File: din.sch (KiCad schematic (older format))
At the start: 1 part, among them J100 C96

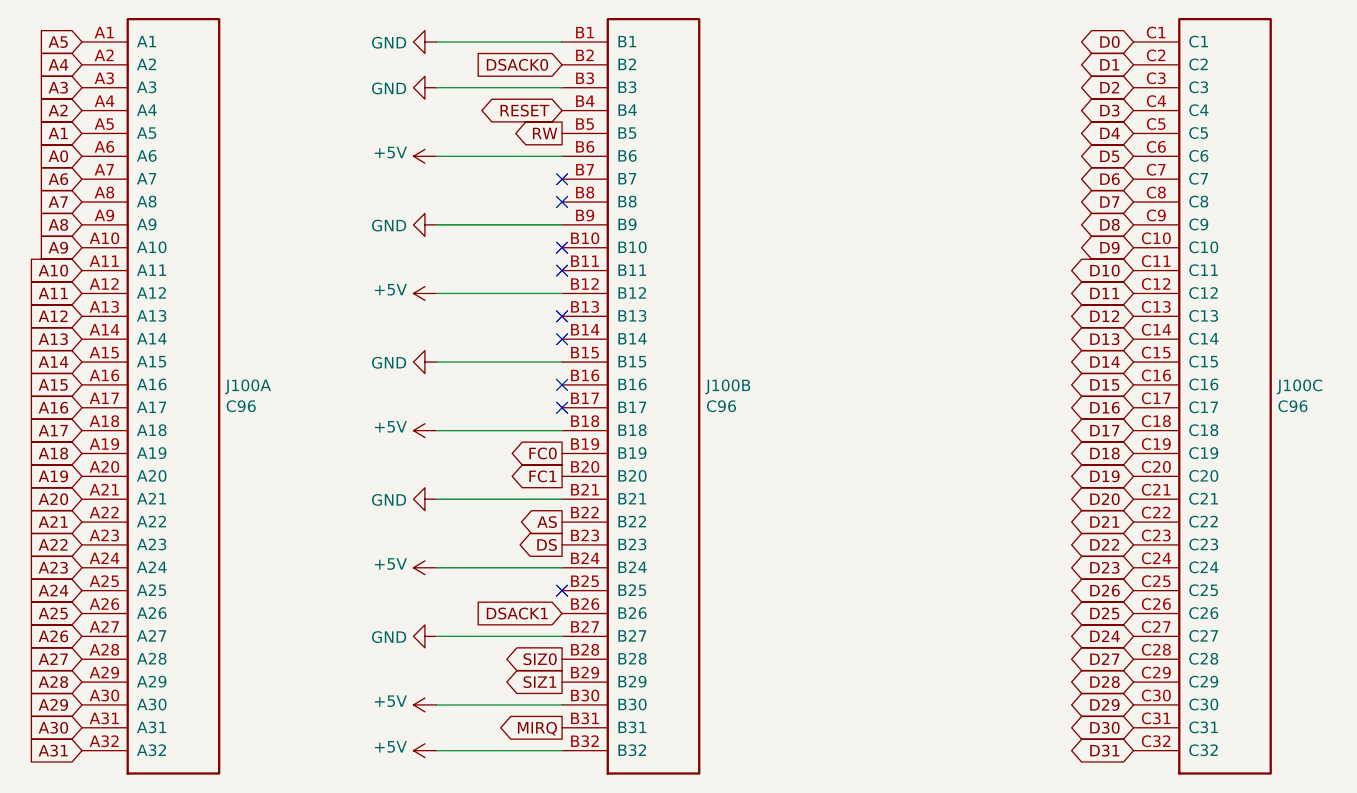
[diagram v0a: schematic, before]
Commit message: updated schematic and initial bga fanout
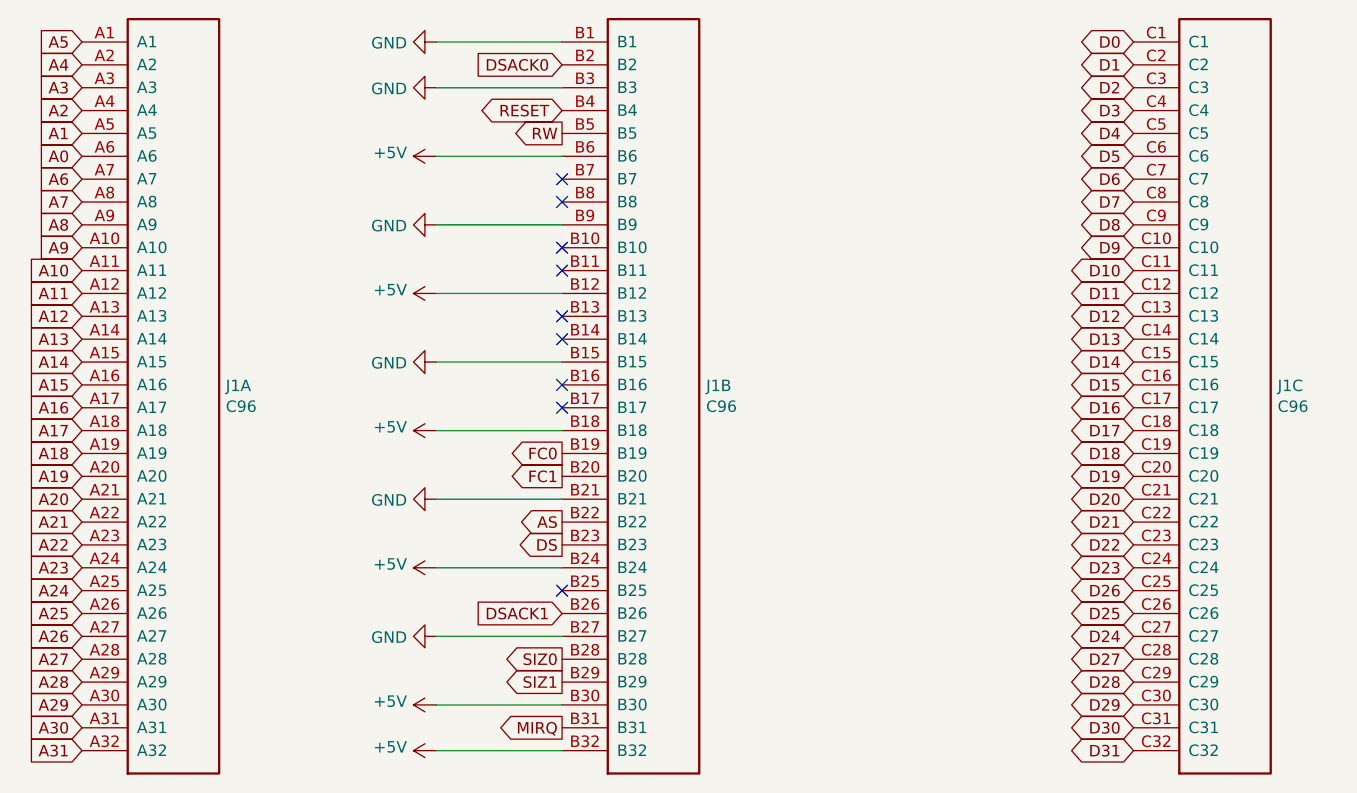
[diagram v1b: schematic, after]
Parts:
- renumbered J100 to J1
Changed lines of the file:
@@
 $Descr A4 11693 8268
 encoding utf-8
-Sheet 2 4
+Sheet 2 7
 Title ""
 Date ""
@@
 $EndDescr
 $Comp
-L parts:C96 J100
+L parts:C96 J1
 U 1 1 5BE0A47E
 P 2400 3150
-F 0 "J100" H 2629 3196 50  0000 L CNN
+F 0 "J1" H 2629 3196 50  0000 L CNN
 F 1 "C96" H 2629 3105 50  0000 L CNN
 F 2 "parts:C96ABCM" H 2400 3150 50  0001 C CNN
@@
 $EndComp
 $Comp
-L parts:C96 J100
+L parts:C96 J1
 U 2 1 5BE0A507
 P 4500 3150
-F 0 "J100" H 4730 3196 50  0000 L CNN
+F 0 "J1" H 4730 3196 50  0000 L CNN
 F 1 "C96" H 4730 3105 50  0000 L CNN
 F 2 "parts:C96ABCM" H 4500 3150 50  0001 C CNN
@@
 $EndComp
 $Comp
-L parts:C96 J100
+L parts:C96 J1
 U 3 1 5BE0A55E
 P 7000 3150
-F 0 "J100" H 7230 3196 50  0000 L CNN
+F 0 "J1" H 7230 3196 50  0000 L CNN
 F 1 "C96" H 7230 3105 50  0000 L CNN
 F 2 "parts:C96ABCM" H 7000 3150 50  0001 C CNN
